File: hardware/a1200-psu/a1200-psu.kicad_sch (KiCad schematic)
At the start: 59 parts, among them J1 220V, J2 Conn_01x05, Q1 P2N60, SW1 SW_SPST, U1 UC3844_DIP8, U2 PC817, U3 TL431D

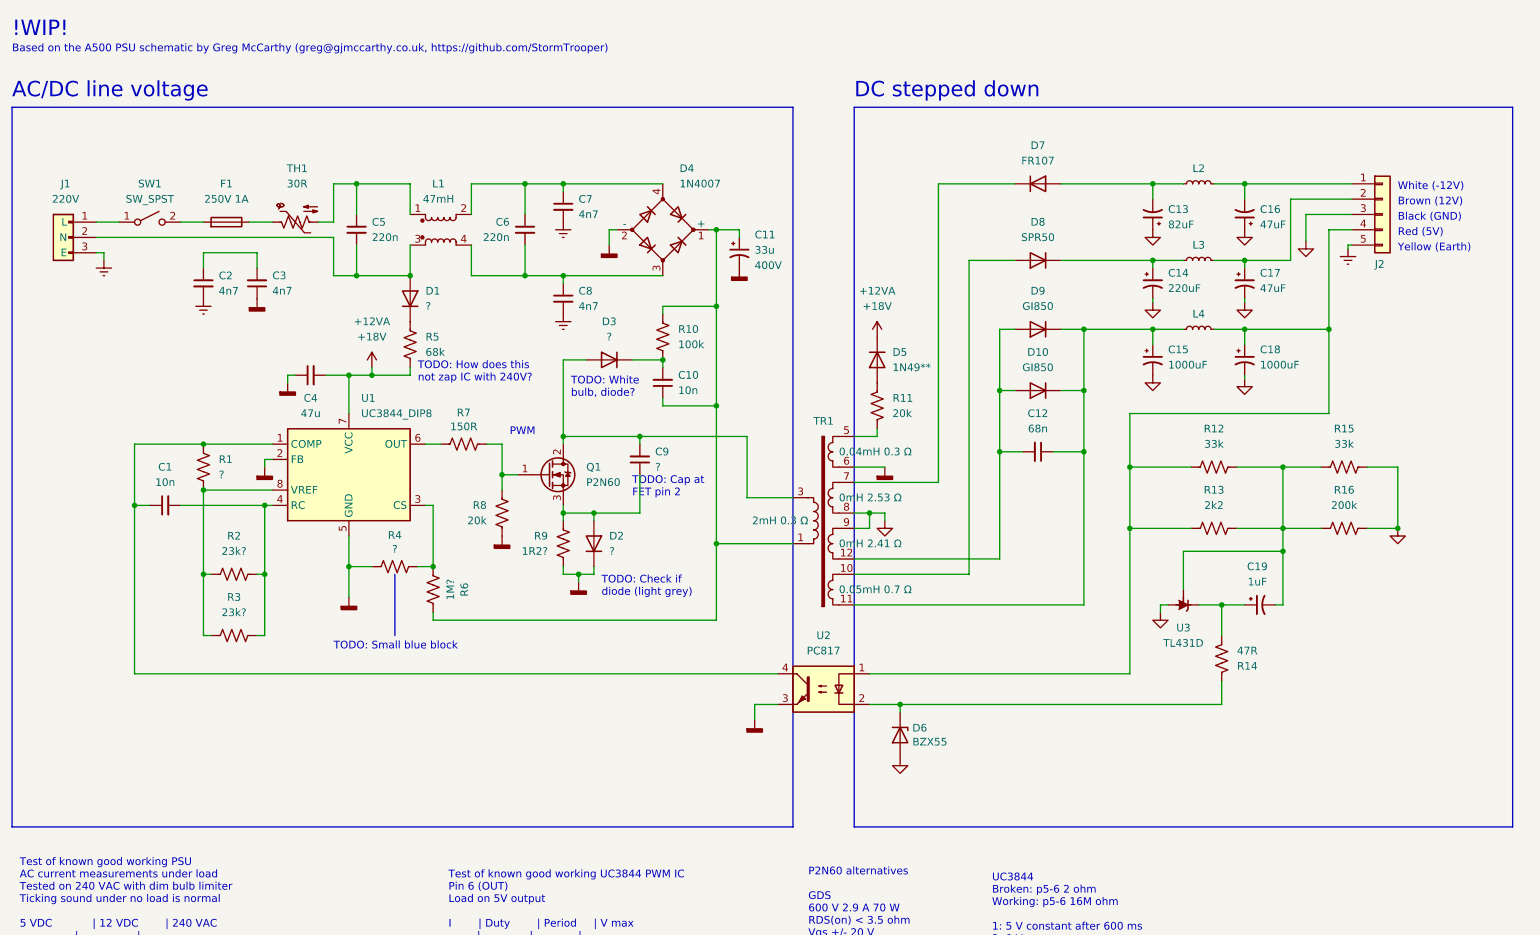
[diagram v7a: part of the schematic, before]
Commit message: Reorganised step down side
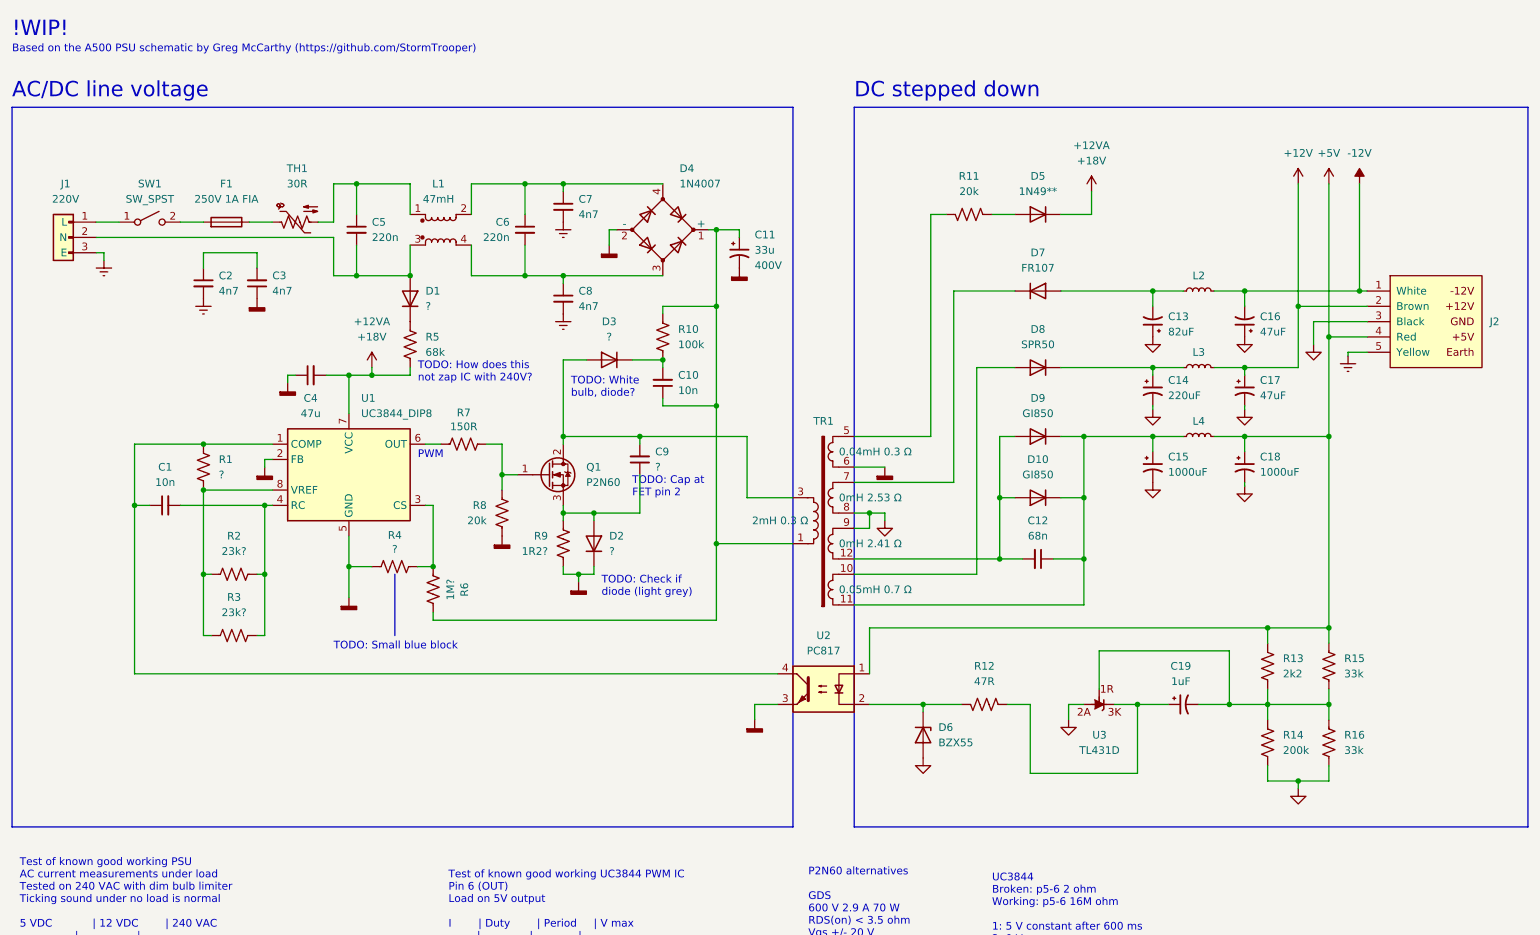
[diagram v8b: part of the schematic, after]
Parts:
- F1: value 250V 1A -> 250V 1A FIA
- J2: symbol Connector_Generic:Conn_01x05 -> Amiga 1200:DC-Out
- R12: value 33k -> 47R
- R14: value 47R -> 200k
- R16: value 200k -> 33k
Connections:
- net GND: now also R14.1; no longer R15.1
- net -12V: now reaches C16.2, J2.1 (White), L2.2
- net +12V: now reaches C17.1, J2.2 (Brown), L3.2
- net +5V: now reaches C18.1, J2.4 (Red), L4.2, R13.2, U2.1
- net +5V: now also R15.2; no longer R12.2
- net at D6.1 (K), U2.2: now also R12.1; no longer R14.2
- net at C19.1, U3.1 (K): now also R12.2; no longer R14.1
- net at C19.2, R13.1, R16.2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: now also R14.2, R15.1; no longer R12.1, R15.2
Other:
- note added: "Based on the A500 PSU schematic by Greg McCarthy (https://github.com/StormTrooper)"
- note removed: "Based on the A500 PSU schematic by Greg McCarthy (greg@gjmccarthy.co.uk, https://github.com/StormTrooper)"
- note removed: "Black (GND)"
- note removed: "Brown (12V)"
- note removed: "Red (5V)"
- note removed: "White (-12V)"
- note removed: "Yellow (Earth)"
- moved on the sheet: C12, C13, C14, C15, C16, C17, C18, D10, D6, D7, D8, D9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
